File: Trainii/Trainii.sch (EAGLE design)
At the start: 35 parts, among them J1 APDS-9960, J2 Left Mtr Encoder, J3 Right Mtr Encoder, J4 Line Sensor 1, J5 Line Sensor 2, J6 Ultrasonic, J7 Left Motor, J8 Right Motor, J9 Lift Motor, M1 ESP32, T1 MCH3383SC-70FL, T2 MCH3383SC-70FL, T3 MCH3383SC-70FL, U1 TPS61222DCKR, U2 BSS138, X1 JST-PH2

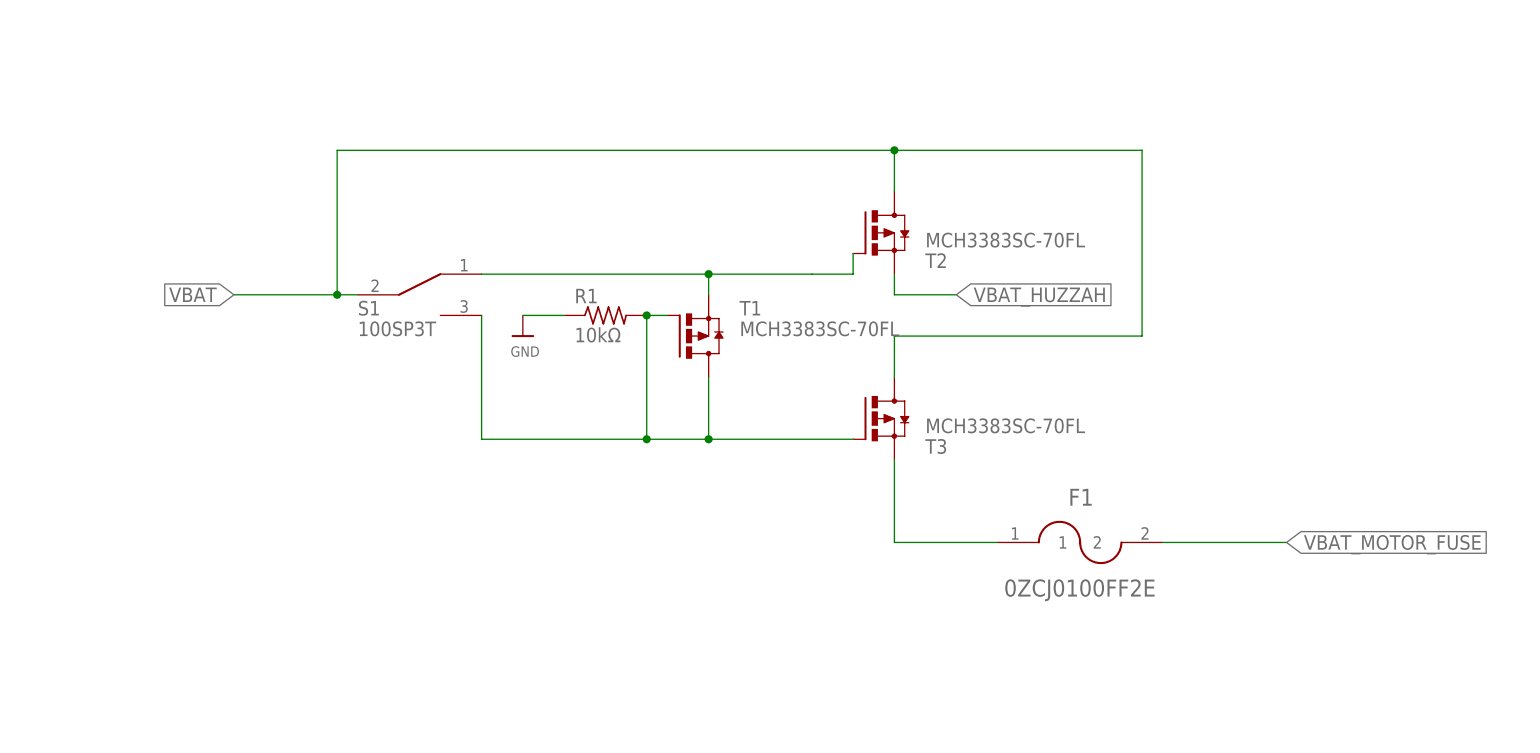
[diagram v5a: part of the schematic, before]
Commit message: Removed additional transistor to allow for charging to work correctly
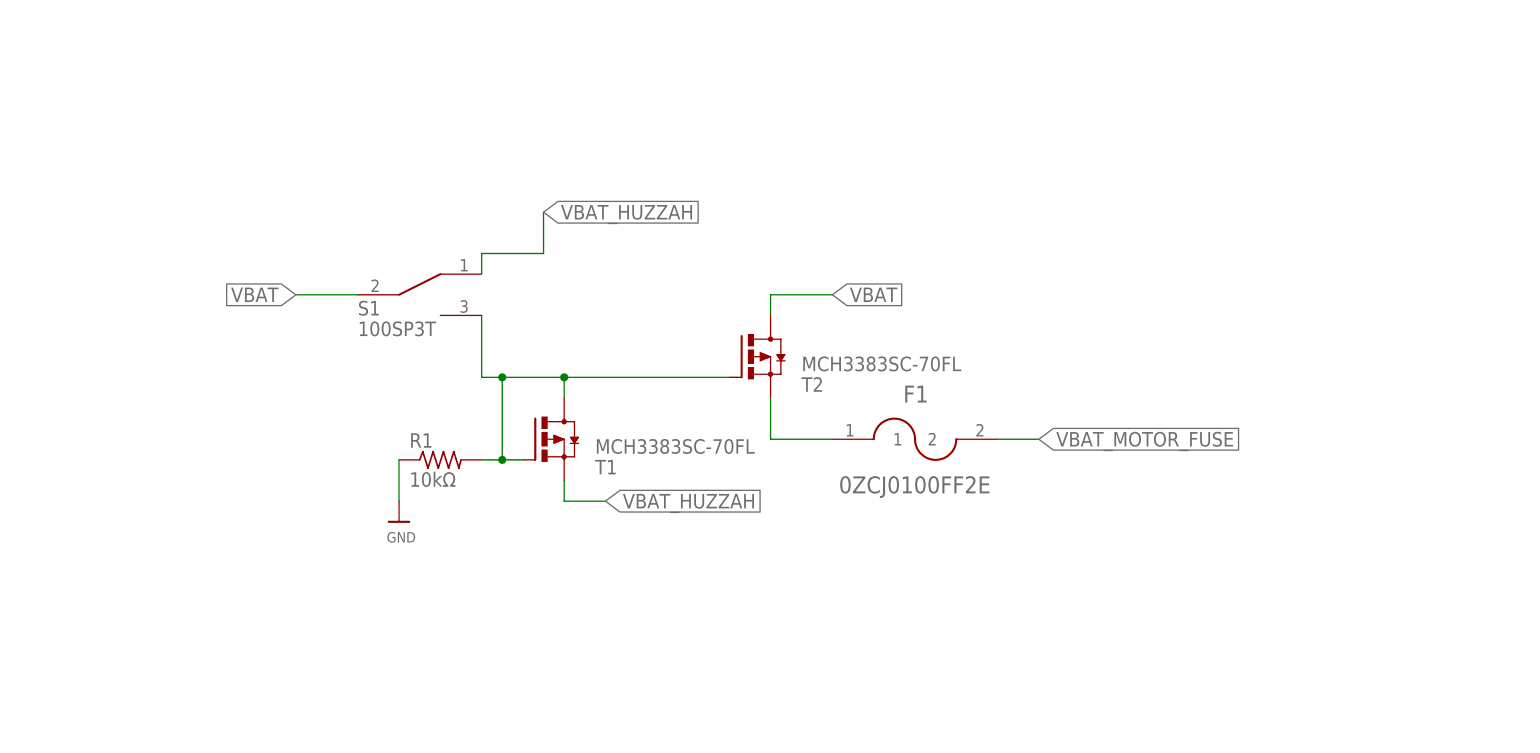
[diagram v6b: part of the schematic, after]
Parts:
- removed T3: MCH3383SC-70FL, Trainii:MCH3383SC-70FL
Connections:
- removed net N$13: R1.2, S1.B, T1.D, T1.G, T3.G
- removed net N$3: S1.A, T1.S, T2.G
- new net N$2: R1.2, S1.B, T1.D, T1.G, T2.G
- net VBAT: no longer T3.D
- net VBAT_HUZZAH: now also S1.A, T1.S; no longer T2.S
- net VBAT_MOTOR: now also T2.S; no longer T3.S
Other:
- moved on the sheet: F1, R1, T1, T2
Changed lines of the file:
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@@
 <part name="F1" library="Trainii" deviceset="0ZCJ0100FF2E" device=""/>
 <part name="T2" library="Trainii" deviceset="MCH3383" device="SC-70FL" package3d_urn="urn:adsk.eagle:package:4252167/1"/>
-<part name="T3" library="Trainii" deviceset="MCH3383" device="SC-70FL" package3d_urn="urn:adsk.eagle:package:4252167/1"/>
 <part name="T1" library="Trainii" deviceset="MCH3383" device="SC-70FL" package3d_urn="urn:adsk.eagle:package:4252167/1"/>
 <part name="R1" library="rcl" library_urn="urn:adsk.eagle:library:334" deviceset="R-US_" device="R0805" package3d_urn="urn:adsk.eagle:package:23553/2" value="10kΩ"/>
@@
 <instance part="X1" gate="G$1" x="254" y="228.6"/>
 <instance part="S1" gate="G$1" x="320.04" y="182.88"/>
-<instance part="F1" gate="G$1" x="401.32" y="152.4"/>
-<instance part="T2" gate="G$1" x="375.92" y="190.5" rot="MR180"/>
-<instance part="T3" gate="G$1" x="375.92" y="167.64" rot="MR180"/>
-<instance part="T1" gate="G$1" x="353.06" y="177.8"/>
-<instance part="R1" gate="G$1" x="342.9" y="180.34"/>
+<instance part="F1" gate="G$1" x="381" y="165.1"/>
+<instance part="T2" gate="G$1" x="360.68" y="175.26" rot="MR180"/>
+<instance part="T1" gate="G$1" x="335.28" y="165.1" rot="MR180"/>
+<instance part="R1" gate="G$1" x="322.58" y="162.56"/>
 <instance part="U$19" gate="G$1" x="254" y="241.3"/>
-<instance part="U$20" gate="G$1" x="332.74" y="177.8"/>
+<instance part="U$20" gate="G$1" x="317.5" y="154.94"/>
 <instance part="J7" gate="G$1" x="121.92" y="104.14"/>
 <instance part="J8" gate="G$1" x="154.94" y="104.14"/>
@@
 <pinref part="R1" gate="G$1" pin="1"/>
 <pinref part="U$20" gate="G$1" pin="GND"/>
-<wire x1="332.74" y1="180.34" x2="337.82" y2="180.34" width="0.1524" layer="91"/>
+<wire x1="317.5" y1="157.48" x2="317.5" y2="162.56" width="0.1524" layer="91"/>
 </segment>
 <segment>
@@
 <net name="VBAT" class="0">
 <segment>
-<pinref part="S1" gate="G$1" pin="COMMON"/>
-<pinref part="T2" gate="G$1" pin="D"/>
-<wire x1="309.88" y1="182.88" x2="312.42" y2="182.88" width="0.1524" layer="91"/>
-<wire x1="378.46" y1="195.58" x2="378.46" y2="200.66" width="0.1524" layer="91"/>
-<wire x1="378.46" y1="200.66" x2="309.88" y2="200.66" width="0.1524" layer="91"/>
-<wire x1="309.88" y1="200.66" x2="309.88" y2="182.88" width="0.1524" layer="91"/>
-<wire x1="378.46" y1="200.66" x2="408.94" y2="200.66" width="0.1524" layer="91"/>
-<junction x="378.46" y="200.66"/>
-<wire x1="408.94" y1="200.66" x2="408.94" y2="177.8" width="0.1524" layer="91"/>
-<wire x1="408.94" y1="177.8" x2="378.46" y2="177.8" width="0.1524" layer="91"/>
-<pinref part="T3" gate="G$1" pin="D"/>
-<wire x1="378.46" y1="177.8" x2="378.46" y2="172.72" width="0.1524" layer="91"/>
-<label x="297.18" y="182.88" size="1.778" layer="95" rot="R180" xref="yes"/>
-<wire x1="309.88" y1="182.88" x2="297.18" y2="182.88" width="0.1524" layer="91"/>
-<junction x="309.88" y="182.88"/>
-</segment>
-<segment>
 <pinref part="X1" gate="G$1" pin="2"/>
 <wire x1="251.46" y1="228.6" x2="251.46" y2="220.98" width="0.1524" layer="91"/>
 <label x="251.46" y="220.98" size="1.778" layer="95" xref="yes"/>
+</segment>
+<segment>
+<pinref part="S1" gate="G$1" pin="COMMON"/>
+<wire x1="312.42" y1="182.88" x2="304.8" y2="182.88" width="0.1524" layer="91"/>
+<label x="304.8" y="182.88" size="1.778" layer="95" rot="R180" xref="yes"/>
+</segment>
+<segment>
+<pinref part="T2" gate="G$1" pin="D"/>
+<wire x1="370.84" y1="182.88" x2="363.22" y2="182.88" width="0.1524" layer="91"/>
+<wire x1="363.22" y1="182.88" x2="363.22" y2="180.34" width="0.1524" layer="91"/>
+<label x="370.84" y="182.88" size="1.778" layer="95" xref="yes"/>
 </segment>
 </net>
@@
 </segment>
 </net>
-<net name="N$3" class="0">
-<segment>
-<pinref part="T2" gate="G$1" pin="G"/>
-<wire x1="373.38" y1="187.96" x2="373.38" y2="185.42" width="0.1524" layer="91"/>
-<pinref part="S1" gate="G$1" pin="A"/>
-<wire x1="373.38" y1="185.42" x2="368.3" y2="185.42" width="0.1524" layer="91"/>
-<wire x1="368.3" y1="185.42" x2="355.6" y2="185.42" width="0.1524" layer="91"/>
-<pinref part="T1" gate="G$1" pin="S"/>
-<wire x1="355.6" y1="185.42" x2="327.66" y2="185.42" width="0.1524" layer="91"/>
-<wire x1="355.6" y1="182.88" x2="355.6" y2="185.42" width="0.1524" layer="91"/>
-<junction x="355.6" y="185.42"/>
-</segment>
-</net>
 <net name="VBAT_MOTOR" class="0">
 <segment>
-<pinref part="T3" gate="G$1" pin="S"/>
-<wire x1="378.46" y1="162.56" x2="378.46" y2="152.4" width="0.1524" layer="91"/>
-<wire x1="378.46" y1="152.4" x2="391.16" y2="152.4" width="0.1524" layer="91"/>
+<pinref part="T2" gate="G$1" pin="S"/>
+<wire x1="363.22" y1="170.18" x2="363.22" y2="165.1" width="0.1524" layer="91"/>
+<wire x1="363.22" y1="165.1" x2="370.84" y2="165.1" width="0.1524" layer="91"/>
 <pinref part="F1" gate="G$1" pin="1"/>
 </segment>
 </net>
-<net name="N$13" class="0">
-<segment>
-<pinref part="R1" gate="G$1" pin="2"/>
-<pinref part="T1" gate="G$1" pin="G"/>
-<wire x1="350.52" y1="180.34" x2="347.98" y2="180.34" width="0.1524" layer="91"/>
-<pinref part="T3" gate="G$1" pin="G"/>
-<pinref part="T1" gate="G$1" pin="D"/>
-<wire x1="355.6" y1="172.72" x2="355.6" y2="165.1" width="0.1524" layer="91"/>
-<wire x1="355.6" y1="165.1" x2="373.38" y2="165.1" width="0.1524" layer="91"/>
-<pinref part="S1" gate="G$1" pin="B"/>
-<wire x1="327.66" y1="180.34" x2="327.66" y2="165.1" width="0.1524" layer="91"/>
-<wire x1="327.66" y1="165.1" x2="347.98" y2="165.1" width="0.1524" layer="91"/>
-<junction x="355.6" y="165.1"/>
-<wire x1="347.98" y1="165.1" x2="355.6" y2="165.1" width="0.1524" layer="91"/>
-<wire x1="347.98" y1="180.34" x2="347.98" y2="165.1" width="0.1524" layer="91"/>
-<junction x="347.98" y="180.34"/>
-<junction x="347.98" y="165.1"/>
-</segment>
-</net>
 <net name="VBAT_MOTOR_FUSE" class="0">
 <segment>
 <pinref part="F1" gate="G$1" pin="2"/>
-<wire x1="411.48" y1="152.4" x2="426.72" y2="152.4" width="0.1524" layer="91"/>
-<label x="426.72" y="152.4" size="1.778" layer="95" xref="yes"/>
+<wire x1="391.16" y1="165.1" x2="396.24" y2="165.1" width="0.1524" layer="91"/>
+<label x="396.24" y="165.1" size="1.778" layer="95" xref="yes"/>
 </segment>
 <segment>
@@
 </segment>
 <segment>
-<pinref part="T2" gate="G$1" pin="S"/>
-<wire x1="378.46" y1="185.42" x2="378.46" y2="182.88" width="0.1524" layer="91"/>
-<label x="386.08" y="182.88" size="1.778" layer="95" xref="yes"/>
-<wire x1="378.46" y1="182.88" x2="386.08" y2="182.88" width="0.1524" layer="91"/>
-</segment>
-</net>
+<pinref part="S1" gate="G$1" pin="A"/>
+<wire x1="335.28" y1="193.04" x2="335.28" y2="187.96" width="0.1524" layer="91"/>
+<wire x1="335.28" y1="187.96" x2="327.66" y2="187.96" width="0.1524" layer="91"/>
+<wire x1="327.66" y1="187.96" x2="327.66" y2="185.42" width="0.1524" layer="91"/>
+<label x="335.28" y="193.04" size="1.778" layer="95" xref="yes"/>
+</segment>
+<segment>
+<pinref part="T1" gate="G$1" pin="S"/>
+<wire x1="337.82" y1="160.02" x2="337.82" y2="157.48" width="0.1524" layer="91"/>
+<wire x1="337.82" y1="157.48" x2="342.9" y2="157.48" width="0.1524" layer="91"/>
+<label x="342.9" y="157.48" size="1.778" layer="95" xref="yes"/>
+</segment>
+</net>
+<net name="N$2" class="0">
+<segment>
+<pinref part="R1" gate="G$1" pin="2"/>
+<pinref part="T1" gate="G$1" pin="G"/>
+<wire x1="332.74" y1="162.56" x2="330.2" y2="162.56" width="0.1524" layer="91"/>
+<pinref part="T2" gate="G$1" pin="G"/>
+<pinref part="S1" gate="G$1" pin="B"/>
+<wire x1="330.2" y1="162.56" x2="327.66" y2="162.56" width="0.1524" layer="91"/>
+<wire x1="337.82" y1="172.72" x2="358.14" y2="172.72" width="0.1524" layer="91"/>
+<wire x1="327.66" y1="180.34" x2="327.66" y2="172.72" width="0.1524" layer="91"/>
+<wire x1="327.66" y1="172.72" x2="330.2" y2="172.72" width="0.1524" layer="91"/>
+<pinref part="T1" gate="G$1" pin="D"/>
+<wire x1="330.2" y1="172.72" x2="337.82" y2="172.72" width="0.1524" layer="91"/>
+<wire x1="337.82" y1="170.18" x2="337.82" y2="172.72" width="0.1524" layer="91"/>
+<junction x="337.82" y="172.72"/>
+<wire x1="330.2" y1="162.56" x2="330.2" y2="172.72" width="0.1524" layer="91"/>
+<junction x="330.2" y="162.56"/>
+<junction x="330.2" y="172.72"/>
+</segment>
+</net>
